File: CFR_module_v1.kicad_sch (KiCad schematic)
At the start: 25 parts, among them J6 Conn_01x20, J7 Conn_01x03, J8 Conn_01x20

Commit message: Modifs
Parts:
- removed A1, A2: Conn_01x04_Pin, Connector_PinHeader_2.54mm:PinHeader_1x04_P2.54mm_Vertical, symbol Connector:Conn_01x04_Pin
- removed ALM1: Conn_01x04_Pin, Connector_JST:JST_EH_B4B-EH-A_1x04_P2.50mm_Vertical, symbol Connector:Conn_01x04_Pin
- removed C2: 100uF/35V, Capacitor_THT:CP_Radial_D6.3mm_P2.50mm, symbol Device:C_Polarized
- removed J6, J8: Conn_01x20, Connector_PinSocket_2.54mm:PinSocket_1x20_P2.54mm_Vertical, symbol Connector_Generic:Conn_01x20
- removed JP1, JP3, JP7, JP9: Conn_01x03_Pin, Connector_PinSocket_2.54mm:PinSocket_1x03_P2.54mm_Vertical, symbol Connector:Conn_01x03_Pin
- removed JP10, JP2, JP4, JP8: Conn_01x02_Pin, Connector_PinSocket_2.54mm:PinSocket_1x02_P2.54mm_Vertical, symbol Connector:Conn_01x02_Pin
- removed MOT1, MOT2, S1, S2: Conn_01x04_Pin, Connector_PinSocket_2.54mm:PinSocket_1x04_P2.54mm_Vertical, symbol Connector:Conn_01x04_Pin
- added ALM1, ALM2, ALM3: Conn_01x02, symbol Connector_Generic:Conn_01x02
- added C1: C_Polarized, symbol Device:C_Polarized
- added C3, C4: 100uF/35V, Capacitor_THT:CP_Radial_D6.3mm_P2.50mm, symbol Device:C_Polarized
- added D1, D2, D3, D4, D6: D, symbol Device:D
- added DBG1: Conn_01x02_Socket, symbol Connector:Conn_01x02_Socket
- added DR3: Pololu_Breakout, Custom:Pololu_Breakout-16_15.2x20.3mm_Better_Silkscreen, symbol Custom:Pololu_Breakout_Stepper_Driver
- added F1: Fuse, symbol Device:Fuse
- added IO1, IO2, MOT1, MOT2, MOT3: Conn_01x04, symbol Connector_Generic:Conn_01x04
- added IO3, IO4, IO5: Conn_01x03, symbol Connector_Generic:Conn_01x03
- added J1, J2: Conn_01x20, Connector_PinSocket_2.54mm:PinSocket_1x20_P2.54mm_Vertical, symbol Connector_Generic:Conn_01x20
- added JP1, JP10, JP11, JP13, JP14, JP2, JP3, JP4, JP5, JP6, JP7, JP8, JP9: Jumper_3_Bridged12, symbol Jumper:Jumper_3_Bridged12
- added R2, R3, R4: 1k, Resistor_THT:R_Axial_DIN0207_L6.3mm_D2.5mm_P7.62mm_Horizontal, symbol Device:R
- renumbered C1 to C2
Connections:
- net +3V3_Pico: now also DR3.10 (MS1), DR3.2 (VDD), J2.5 (Pin_5), JP13.1 (A); no longer DR1.11 (MS2)
- net +5V: now also ALM3.1 (Pin_1), JP13.3 (B), JP14.1 (A)
- net +9V: now also ALM2.1 (Pin_1), JP14.3 (B)
- net +BATT: now also C1.2, C3.1, C4.1, DR3.8 (VMOT), F1.1
- net 3V3_EN: now also J2.4 (Pin_4)
- net ADC_VREF: now also J2.6 (Pin_6)
- net AGND: now also J2.8 (Pin_8)
- net GND: now also DR1.11 (MS2), ALM1.2 (Pin_2), ALM2.2 (Pin_2), ALM3.2 (Pin_2), C1.1, C3.2, C4.2, D1.2 (A), D2.2 (A), D3.2 (A), D4.2 (A), D6.2 (A), DR3.1 (GND), DR3.11 (MS2), DR3.7 (GND), IO1.1 (Pin_1), IO2.1 (Pin_1), IO3.1 (Pin_1), IO4.1 (Pin_1), IO5.1 (Pin_1), J1.13 (Pin_13), J1.18 (Pin_18), J1.3 (Pin_3), J1.8 (Pin_8), J2.13 (Pin_13), J2.18 (Pin_18), J2.3 (Pin_3); no longer DR1.14 (~{SLEEP}), DR2.14 (~{SLEEP})
- net GP0: now also DBG1.2 (Pin_2), J1.1 (Pin_1)
- net GP1: now also DBG1.1 (Pin_1), J1.2 (Pin_2)
- net GP12: now also DR2.15 (STEP), J1.16 (Pin_16); no longer DR1.16 (DIR), DR2.16 (DIR)
- net GP13: now also J1.17 (Pin_17), JP4.1 (A); no longer DR1.15 (STEP), DR2.15 (STEP)
- net GP14: now also J1.19 (Pin_19), JP3.1 (A)
- net GP15: now also DR2.9 (~{ENABLE}), J1.20 (Pin_20)
- net GP16: now also J2.20 (Pin_20)
- net GP17: now also J2.19 (Pin_19)
- net GP18: now also DR3.9 (~{ENABLE}), J2.17 (Pin_17)
- net GP19: now also J2.16 (Pin_16), JP5.1 (A)
- net GP2: now also IO1.3 (Pin_3), IO2.3 (Pin_3), J1.4 (Pin_4)
- net GP22: now also DR3.16 (DIR), J2.12 (Pin_12)
- net GP26_A0: now also IO3.3 (Pin_3), J2.10 (Pin_10)
- net GP27_A1: now also IO4.3 (Pin_3), J2.9 (Pin_9)
- net GP28_A2: now also IO5.3 (Pin_3), J2.7 (Pin_7)
- net GP3: now also IO1.4 (Pin_4), IO2.4 (Pin_4), J1.5 (Pin_5)
- net GP4: now also R1.1, J1.6 (Pin_6); no longer R1.2
- net GP5: now also R1.2, J1.7 (Pin_7), JP1.3 (B), JP3.3 (B), JP5.3 (B), R2.1, R3.1, R4.1; no longer DR1.12 (MS3), DR2.12 (MS3), R1.1
- net GP6: now also DR1.16 (DIR), J1.9 (Pin_9); no longer DR1.9 (~{ENABLE}), DR2.9 (~{ENABLE})
- net GP7: now also DR1.15 (STEP), J1.10 (Pin_10)
- net RUN: now also J2.11 (Pin_11)
- net VBUS: now also J2.1 (Pin_1)
- net VSYS: now also J2.2 (Pin_2)
- net at DR2.3 (OB1): now also MOT2.4 (Pin_4)
- net at DR2.4 (OB2): now also MOT2.3 (Pin_3)
- net at DR2.5 (OA2): now also MOT2.2 (Pin_2)
- net at DR2.6 (OA1): now also MOT2.1 (Pin_1)
- net at DR1.3 (OB1): now also MOT1.4 (Pin_4)
- net at DR1.4 (OB2): now also MOT1.3 (Pin_3)
- net at DR1.5 (OA2): now also MOT1.2 (Pin_2)
- net at DR1.6 (OA1): now also MOT1.1 (Pin_1)
- net at DR2.13 (PDN2/IB1): now also JP4.2 (C)
- net at DR1.13 (PDN2/IB1): now also JP2.2 (C)
- net ACT1_0_U1_TX renamed GP8
- net GP8: now also J1.11 (Pin_11), JP2.1 (A)
- net ACT1_1_U1_RX renamed GP9
- net GP9: now also J1.12 (Pin_12), JP1.1 (A)
- net ACT2_0 renamed GP10
- net GP10: now also DR1.9 (~{ENABLE}), J1.14 (Pin_14)
- net ACT2_1 renamed GP11
- net GP11: now also DR2.16 (DIR), J1.15 (Pin_15)
- net ACT3 renamed GP20
- net GP20: now also J2.15 (Pin_15), JP6.1 (A)
- net ACT4 renamed GP21
- net GP21: now also DR3.15 (STEP), J2.14 (Pin_14)
- new net: D2.1 (K), IO2.2 (Pin_2), JP7.2 (C)
- new net: D4.1 (K), IO4.2 (Pin_2), JP9.2 (C)
- new net: D1.1 (K), IO1.2 (Pin_2), JP11.2 (C)
- new net: JP6.3 (B), R4.2
- new net: DR3.6 (OA1), MOT3.1 (Pin_1)
- new net: DR3.5 (OA2), MOT3.2 (Pin_2)
- new net: DR3.4 (OB2), MOT3.3 (Pin_3)
- new net: DR3.3 (OB1), MOT3.4 (Pin_4)
- new net: D3.1 (K), IO3.2 (Pin_2), JP8.2 (C)
- new net: DR1.12 (PDN1/IB2), JP1.2 (C)
- new net: ALM1.1 (Pin_1), F1.2
- new net: D6.1 (K), IO5.2 (Pin_2), JP10.2 (C)
- new net: DR3.12 (PDN1/IB2), JP5.2 (C)
- new net: DR2.12 (PDN1/IB2), JP3.2 (C)
- new net: DR3.13 (PDN2/IB1), JP6.2 (C)
- new net: JP2.3 (B), R2.2
- new net: JP4.3 (B), R3.2
- new net +V1: JP10.3 (B), JP11.3 (B), JP13.2 (C), JP7.3 (B), JP8.3 (B), JP9.3 (B)
- new net +V2: JP10.1 (A), JP11.1 (A), JP14.2 (C), JP7.1 (A), JP8.1 (A), JP9.1 (A)
- no-connect marks 2 -> 3
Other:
- note added: "Sensors/Actuators"
- note removed: "Actuators"
- note removed: "Sensors"
- moved on the sheet: C2, D5, DR1, Pico0, R1

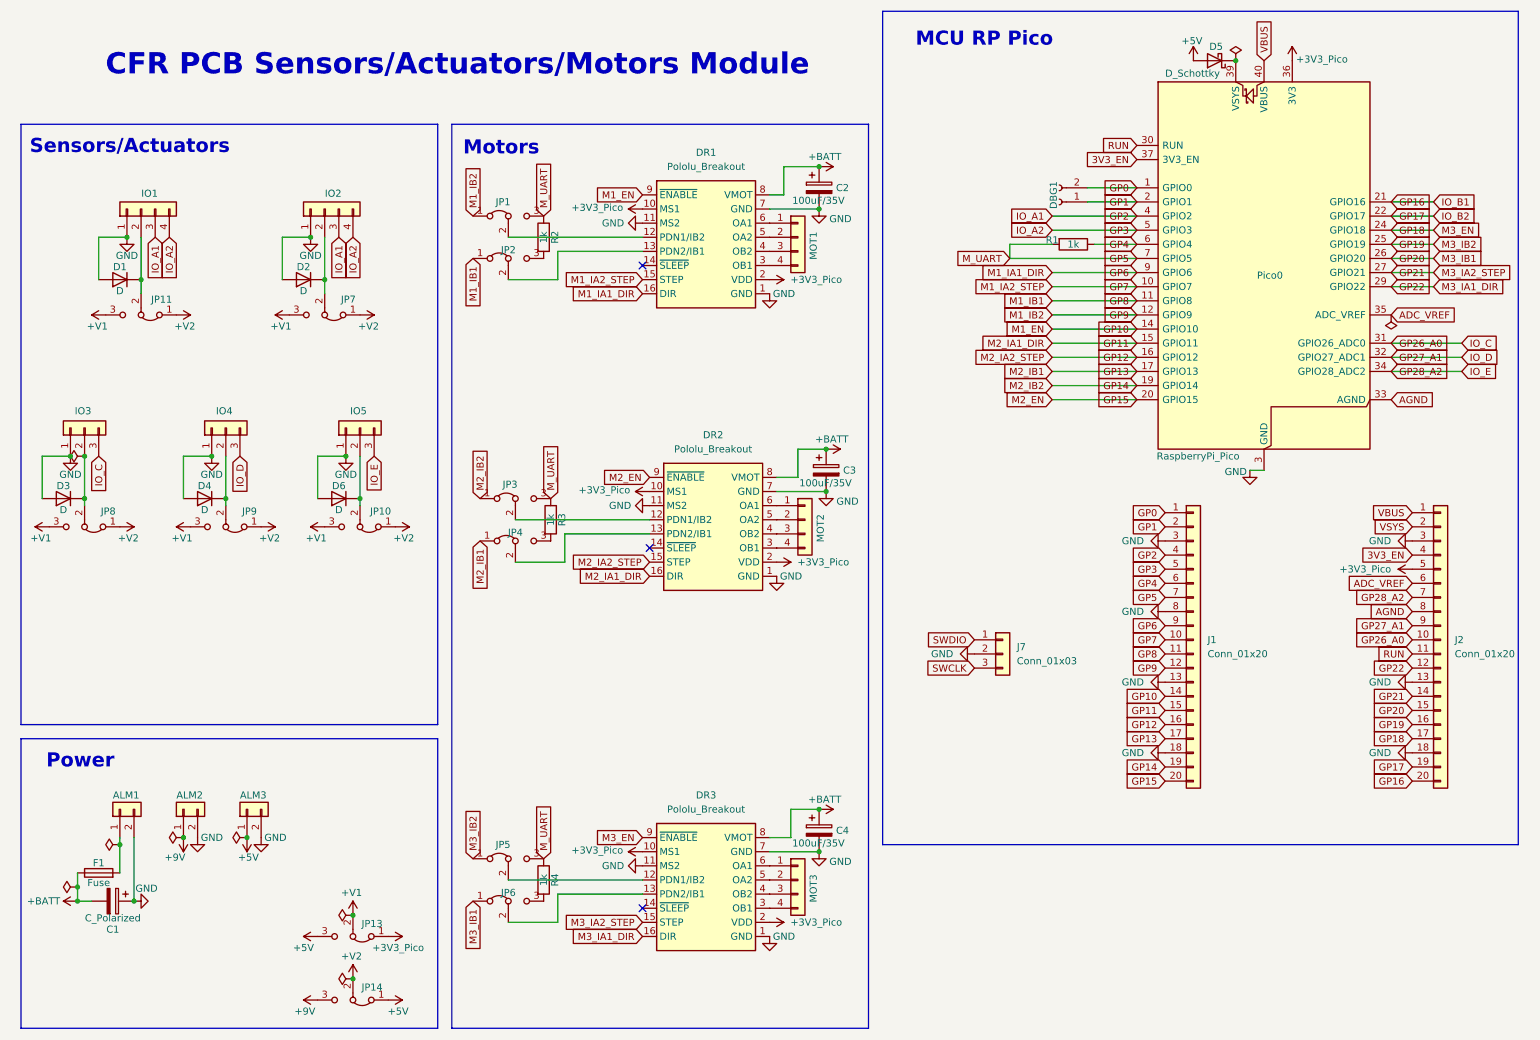
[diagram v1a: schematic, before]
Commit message: v1 du schematics, debut de pcb
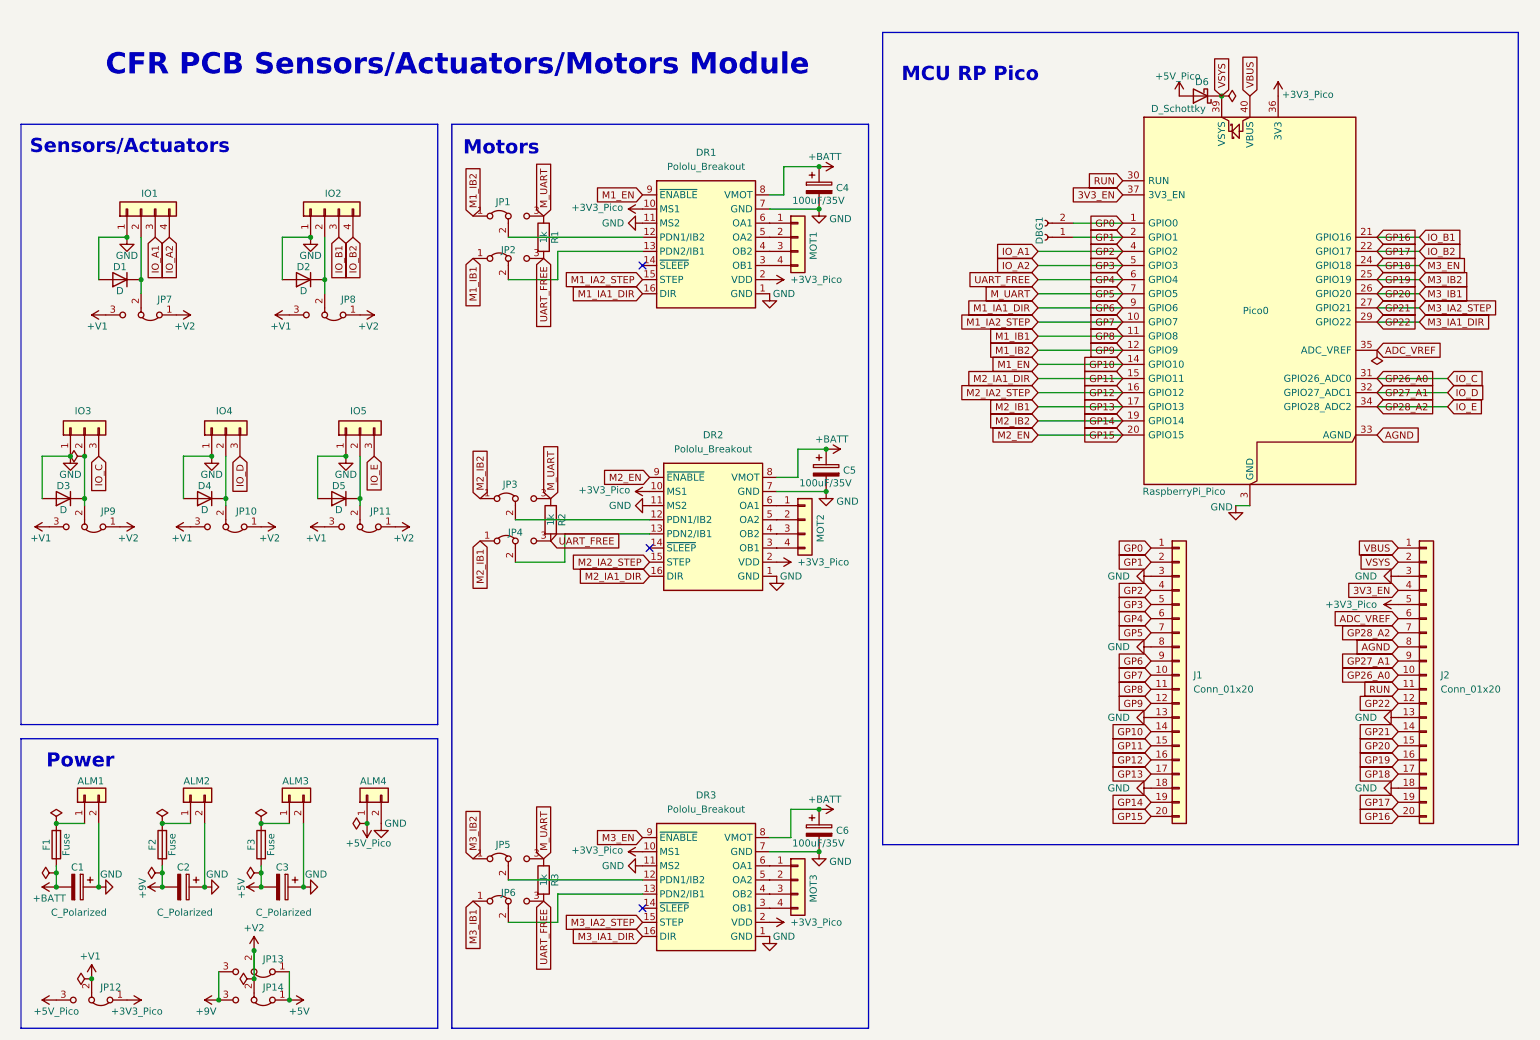
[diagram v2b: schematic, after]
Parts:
- removed J7: Conn_01x03, Connector_PinSocket_2.54mm:PinSocket_1x03_P2.54mm_Vertical, symbol Connector_Generic:Conn_01x03
- removed R1: 1k, Resistor_THT:R_Axial_DIN0207_L6.3mm_D2.5mm_P7.62mm_Horizontal, symbol Device:R
- added ALM3: Conn_01x02, Connector_AMASS:AMASS_XT30U-F_1x02_P5.0mm_Vertical, symbol Connector_Generic:Conn_01x02
- added C2: C_Polarized, Capacitor_SMD:CP_Elec_8x10, symbol Device:C_Polarized
- added C3: C_Polarized, Capacitor_SMD:CP_Elec_6.3x5.8, symbol Device:C_Polarized
- added F2, F3: Fuse, Fuse:Fuse_1206_3216Metric_Pad1.42x1.75mm_HandSolder, symbol Device:Fuse
- added JP13: Jumper_3_Bridged12, Connector_PinHeader_2.54mm:PinHeader_1x03_P2.54mm_Vertical, symbol Jumper:Jumper_3_Bridged12
- ALM1, ALM2: footprint (none) -> Connector_AMASS:AMASS_XT30U-F_1x02_P5.0mm_Vertical
- ALM4: renamed from ALM3; footprint (none) -> Connector_AMASS:AMASS_XT30U-F_1x02_P5.0mm_Vertical
- C1: footprint (none) -> Capacitor_SMD:CP_Elec_10x10.5
- D1, D2, D3, D4: footprint (none) -> Diode_SMD:D_SMA_Handsoldering
- D5: renamed from D6; footprint (none) -> Diode_SMD:D_SMA_Handsoldering
- D6: renamed from D5; footprint Diode_THT:D_DO-41_SOD81_P10.16mm_Horizontal -> Diode_SMD:D_SOD-123
- DBG1: footprint (none) -> Connector_PinHeader_2.54mm:PinHeader_1x02_P2.54mm_Vertical
- F1: footprint (none) -> Fuse:Fuse_1206_3216Metric_Pad1.42x1.75mm_HandSolder
- IO1, IO2: footprint (none) -> Connector_JST:JST_PH_B4B-PH-K_1x04_P2.00mm_Vertical
- IO3, IO4, IO5: footprint (none) -> Connector_JST:JST_PH_B3B-PH-K_1x03_P2.00mm_Vertical
- JP1, JP14, JP2, JP3, JP4, JP5, JP6: footprint (none) -> Connector_PinHeader_2.54mm:PinHeader_1x03_P2.54mm_Vertical
- JP10: renamed from JP9; footprint (none) -> Connector_PinHeader_2.54mm:PinHeader_1x03_P2.54mm_Vertical
- JP11: renamed from JP10; footprint (none) -> Connector_PinHeader_2.54mm:PinHeader_1x03_P2.54mm_Vertical
- JP12: renamed from JP13; footprint (none) -> Connector_PinHeader_2.54mm:PinHeader_1x03_P2.54mm_Vertical
- JP7: renamed from JP11; footprint (none) -> Connector_PinHeader_2.54mm:PinHeader_1x03_P2.54mm_Vertical
- JP8: renamed from JP7; footprint (none) -> Connector_PinHeader_2.54mm:PinHeader_1x03_P2.54mm_Vertical
- JP9: renamed from JP8; footprint (none) -> Connector_PinHeader_2.54mm:PinHeader_1x03_P2.54mm_Vertical
- MOT1, MOT2, MOT3: footprint (none) -> Connector_PinHeader_2.54mm:PinHeader_1x04_P2.54mm_Vertical
- R1: renamed from R2; footprint Resistor_THT:R_Axial_DIN0207_L6.3mm_D2.5mm_P7.62mm_Horizontal -> Resistor_SMD:R_0805_2012Metric_Pad1.20x1.40mm_HandSolder
- R2: renamed from R3; footprint Resistor_THT:R_Axial_DIN0207_L6.3mm_D2.5mm_P7.62mm_Horizontal -> Resistor_SMD:R_0805_2012Metric_Pad1.20x1.40mm_HandSolder
- R3: renamed from R4; footprint Resistor_THT:R_Axial_DIN0207_L6.3mm_D2.5mm_P7.62mm_Horizontal -> Resistor_SMD:R_0805_2012Metric_Pad1.20x1.40mm_HandSolder
- renumbered C2 to C4, C3 to C5, C4 to C6
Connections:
- net +5V: now also C3.2, F3.1, JP13.1 (A); no longer ALM4.1 (Pin_1), D6.2 (A), JP12.3 (B)
- net +9V: now also C2.2, F2.1, JP13.3 (B); no longer ALM2.1 (Pin_1)
- net +V2: now also JP13.2 (C)
- net GND: now also ALM3.2 (Pin_2), C2.1, C3.1
- net GP16: now also IO2.3 (Pin_3)
- net GP17: now also IO2.4 (Pin_4)
- net GP2: no longer IO2.3 (Pin_3)
- net GP3: no longer IO2.4 (Pin_4)
- net GP4: now also JP2.3 (B), JP4.3 (B), JP6.3 (B), R1.2, R2.2, R3.2
- net VSYS: now also D6.1 (K), Pico0.39 (VSYS)
- new net: ALM2.1 (Pin_1), F2.2
- new net: ALM3.1 (Pin_1), F3.2
- new net +5V_Pico: ALM4.1 (Pin_1), D6.2 (A), JP12.3 (B)
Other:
- moved on the sheet: ALM1, ALM2, ALM4, C1, D6, DBG1, F1, J1, J2, JP12, JP14, Pico0

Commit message: pcb ok
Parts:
- removed R2, R3: 1k, Resistor_SMD:R_0805_2012Metric_Pad1.20x1.40mm_HandSolder, symbol Device:R
- C4, C5, C6: footprint Capacitor_THT:CP_Radial_D6.3mm_P2.50mm -> Capacitor_SMD:CP_Elec_6.3x7.7
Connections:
- net +3V3_Pico: now also DR2.11 (MS2); no longer DR1.10 (MS1), DR2.10 (MS1)
- net GND: now also DR1.10 (MS1), DR2.10 (MS1); no longer ALM1.2 (Pin_2), ALM2.2 (Pin_2), ALM3.2 (Pin_2), C1.1, C2.1, C3.1, C4.2, C5.2, C6.2, D1.2 (A), D2.2 (A), D3.2 (A), D4.2 (A), D5.2 (A), DR1.7 (GND), DR2.11 (MS2), DR2.7 (GND), DR3.7 (GND), IO1.1 (Pin_1), IO2.1 (Pin_1), IO3.1 (Pin_1), IO4.1 (Pin_1), IO5.1 (Pin_1)
- net GP18: now also DR3.16 (DIR); no longer DR3.9 (~{ENABLE})
- net GP19: now also DR3.15 (STEP); no longer JP5.1 (A)
- net GP21: now also JP5.1 (A); no longer DR3.15 (STEP)
- net GP22: now also DR3.9 (~{ENABLE}); no longer DR3.16 (DIR)
- net GP4: now also R1.1; no longer JP2.3 (B), JP4.3 (B), JP6.3 (B), R1.2
- net GP5: now also R1.2; no longer R1.1
- new net GNDPWR1: ALM1.2 (Pin_2), C1.1, C4.2, C5.2, C6.2, DR1.7 (GND), DR2.7 (GND), DR3.7 (GND)
- new net GNDPWR2: ALM2.2 (Pin_2), ALM3.2 (Pin_2), C2.1, C3.1, D1.2 (A), D2.2 (A), D3.2 (A), D4.2 (A), D5.2 (A), IO1.1 (Pin_1), IO2.1 (Pin_1), IO3.1 (Pin_1), IO4.1 (Pin_1), IO5.1 (Pin_1)
- no-connect marks 3 -> 6
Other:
- moved on the sheet: R1

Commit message: fini avant modifs
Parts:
- added BAU1: Conn_01x02, Connector_PinHeader_2.54mm:PinHeader_1x02_P2.54mm_Vertical, symbol Connector_Generic:Conn_01x02
- added D10, D11, D12, D7, D8, D9: D_Schottky, Diode_SMD:D_SOD-123, symbol Device:D_Schottky
- added H1, H2, H3, H4: MountingHole, MountingHole:MountingHole_3.2mm_M3, symbol Mechanical:MountingHole
- added Q1: NPN, Package_TO_SOT_SMD:SOT-23, symbol Simulation_SPICE:NPN
- added R2, R4, R5, R6: 1k, Resistor_SMD:R_0805_2012Metric_Pad1.20x1.40mm_HandSolder, symbol Device:R
- added R3: 10k, Resistor_SMD:R_0805_2012Metric_Pad1.20x1.40mm_HandSolder, symbol Device:R
- PiPico0: renamed from Pico0; footprint Module:RaspberryPi_Pico_Common_Unspecified -> Module:RaspberryPi_Pico_Common_SMD
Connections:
- net +3V3_Pico: now also R3.1
- net +5V: now also C3.1; no longer C3.2
- net +9V: now also C2.1; no longer C2.2
- net +BATT: now also C1.1; no longer C1.2
- net GND: now also BAU1.1 (Pin_1), Q1.3 (E)
- net GNDPWR1: now also C1.2; no longer C1.1
- net GNDPWR2: now also C2.2, C3.2; no longer C2.1, C3.1
- net GP10: now also R4.1; no longer DR1.9 (~{ENABLE})
- net GP15: now also R5.1; no longer DR2.9 (~{ENABLE})
- net GP22: now also R6.1; no longer DR3.9 (~{ENABLE})
- new net: D7.2 (A), D8.2 (A), D9.2 (A), Q1.1 (C), R3.2
- new net: BAU1.2 (Pin_2), R2.1
- new net: Q1.2 (B), R2.2
- new net: D12.2 (A), R6.2
- new net: D11.2 (A), R5.2
- new net: D10.2 (A), R4.2
- new net M1_EN: D10.1 (K), D7.1 (K), DR1.9 (~{ENABLE})
- new net M2_EN: D11.1 (K), D8.1 (K), DR2.9 (~{ENABLE})
- new net M3_EN: D12.1 (K), D9.1 (K), DR3.9 (~{ENABLE})
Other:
- moved on the sheet: ALM1, ALM2, ALM3, ALM4, C1, C2, C3, C5, C6, DR2, DR3, F1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
